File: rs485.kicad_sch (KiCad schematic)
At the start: 38 parts, among them J1801 RS485 RX Socket, J1802 RS485 TX Socket, U1801 ISO7721DR, U1802 SN75176BDR, U1803 SN75176BDR

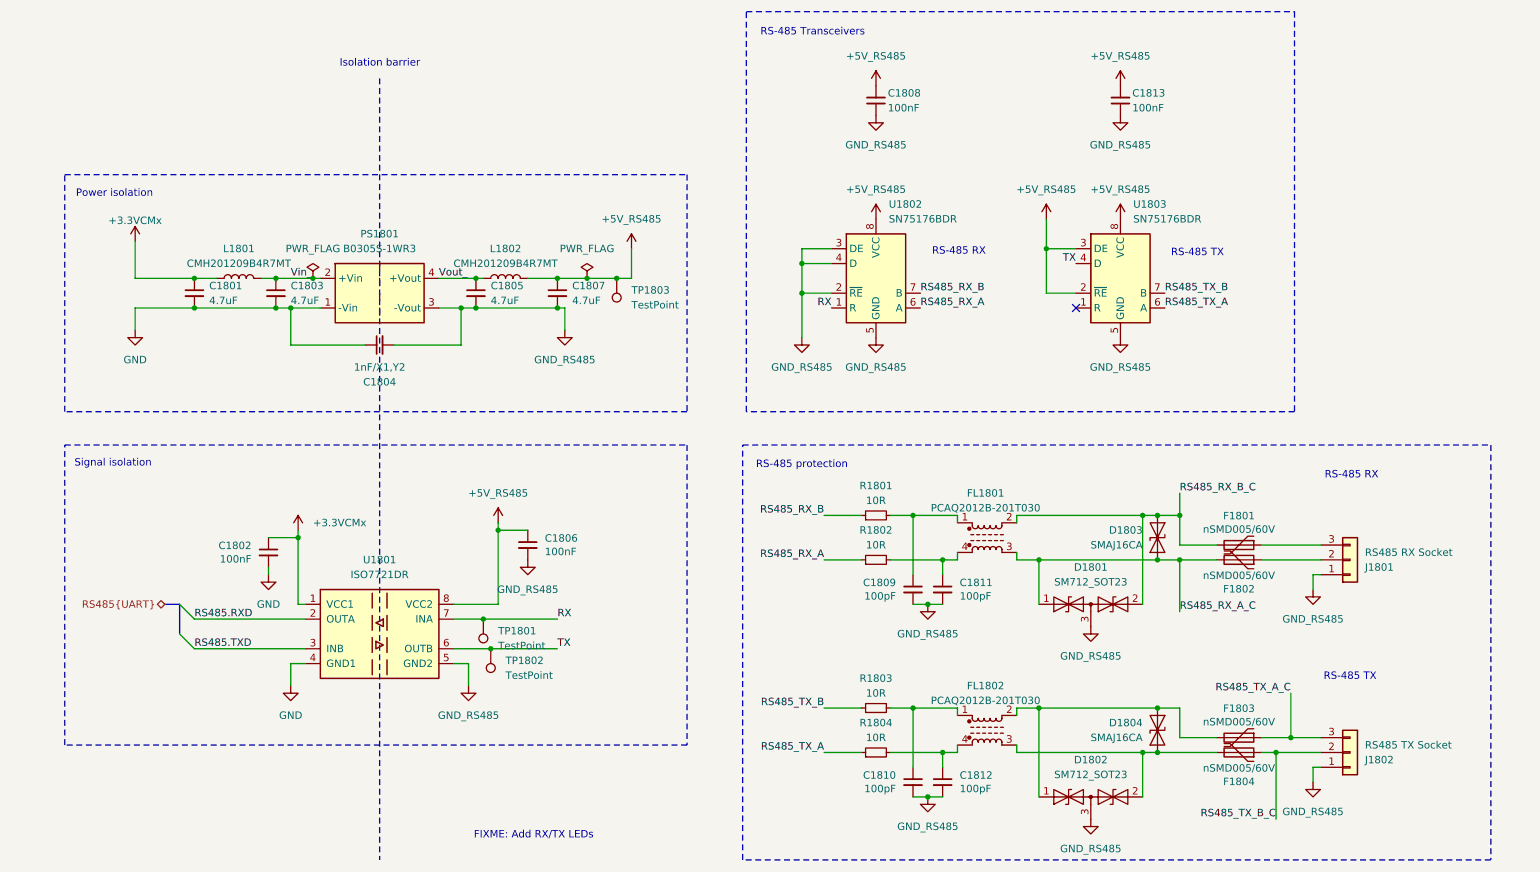
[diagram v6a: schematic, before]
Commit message: Partial trace layout, kick-ass custom rules
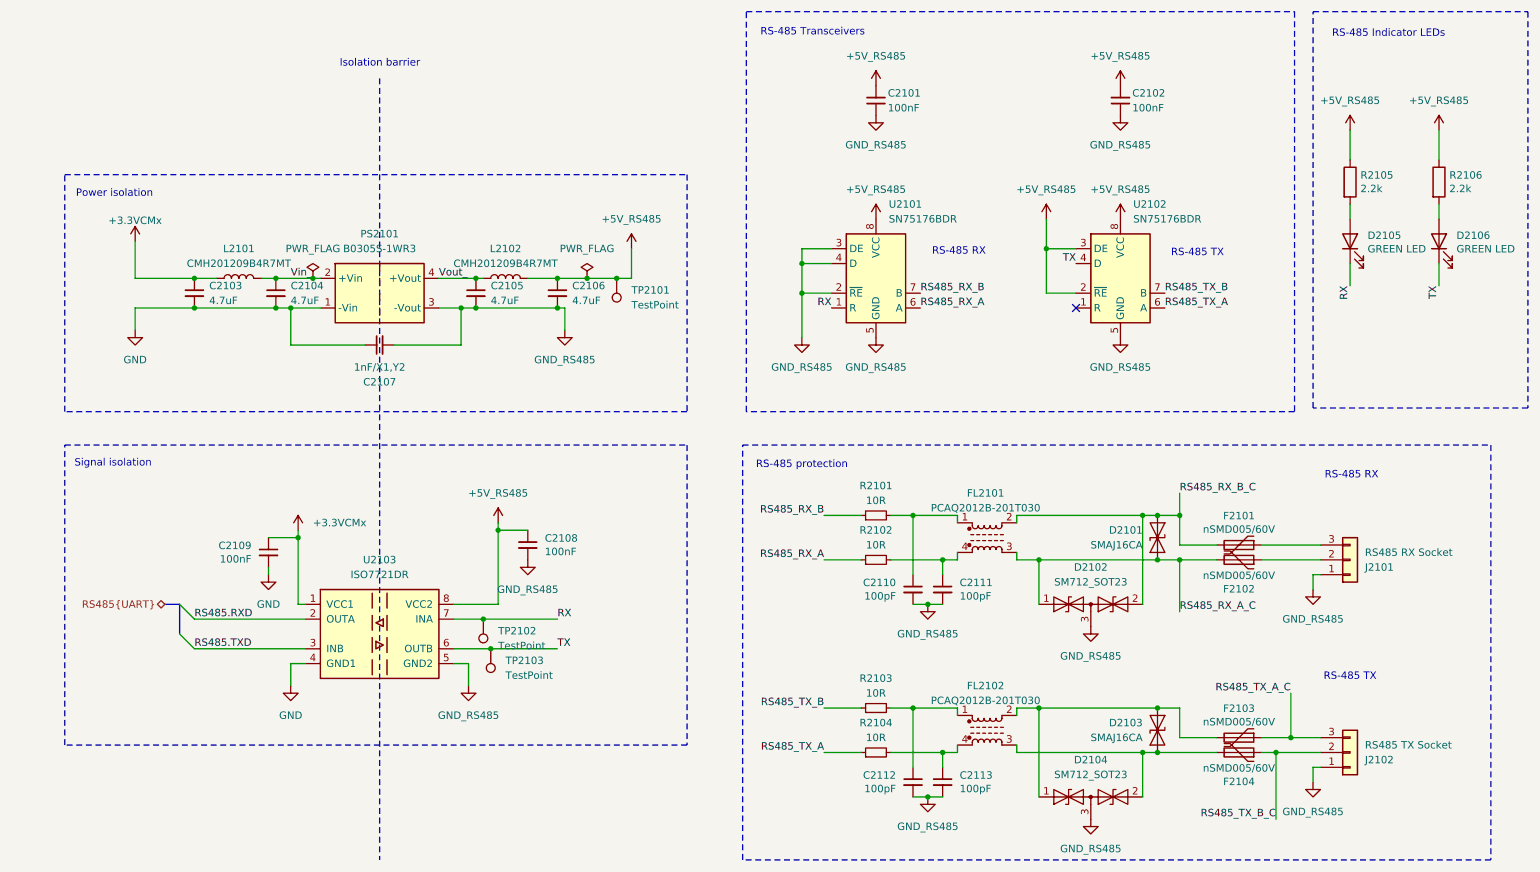
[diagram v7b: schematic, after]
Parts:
- added D2105, D2106: GREEN LED, LED_SMD:LED_0603_1608Metric, symbol Device:LED
- added R2105, R2106: 2.2k, Resistor_SMD:R_0402_1005Metric, symbol Device:R
- renumbered C1808 to C2101, C1813 to C2102, C1801 to C2103, C1803 to C2104, C1805 to C2105, C1807 to C2106, C1804 to C2107, C1806 to C2108, C1802 to C2109, C1809 to C2110, C1811 to C2111, C1810 to C2112, C1812 to C2113, D1803 to D2101, D1801 to D2102, D1804 to D2103, D1802 to D2104, F1801 to F2101, F1802 to F2102, F1803 to F2103, F1804 to F2104, FL1801 to FL2101, FL1802 to FL2102, J1801 to J2101, J1802 to J2102, L1801 to L2101, L1802 to L2102, PS1801 to PS2101, R1801 to R2101, R1802 to R2102, R1803 to R2103, R1804 to R2104, TP1803 to TP2101, TP1801 to TP2102, TP1802 to TP2103, U1802 to U2101, U1803 to U2102, U1801 to U2103
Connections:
- net +5V_RS485: now also R2105.1, R2106.1
- net RX: now also D2105.1 (K)
- net TX: now also D2106.1 (K)
- new net: D2105.2 (A), R2105.2
- new net: D2106.2 (A), R2106.2
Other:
- note added: "RS-485 Indicator LEDs"
- note removed: "FIXME: Add RX/TX LEDs"

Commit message: A big part of layout and routing done
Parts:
- removed J2102: RS485 TX Socket, Connector_Phoenix_MC:PhoenixContact_MCV_1,5_3-G-3.81_1x03_P3.81mm_Vertical, symbol Connector_Generic:Conn_01x03
- removed U2101, U2102: SN75176BDR, PCM_Package_SO_AKL:SOIC-8_3.9x4.9mm_P1.27mm, symbol Interface_UART:SN75176AD
- removed U2103: ISO7721DR, Package_SO:SOIC-8_3.9x4.9mm_P1.27mm, symbol Hatlabs:ISO7721DR
- added U2102: ISO7741DBQ, Package_SO:SSOP-16_3.9x4.9mm_P0.635mm, symbol Hatlabs:ISO7741DBQ
- added U2104, U2105: SP3485EN-L/TR, Package_SO:SOIC-8_3.9x4.9mm_P1.27mm, symbol Interface_UART:SP3485EN
- D2102: footprint PCM_Package_TO_SOT_SMD_AKL:SOT-23 -> Package_TO_SOT_SMD:SOT-23; Component Class (none) -> fine_pitch
- D2104: footprint PCM_Package_TO_SOT_SMD_AKL:SOT-23 -> Package_TO_SOT_SMD:SOT-23
- F2101, F2102, F2103, F2104: footprint PCM_Fuse_AKL:Fuse_1206_3216Metric -> Fuse:Fuse_1206_3216Metric
- J2101: value RS485 RX Socket -> RS485 Socket; footprint Connector_Phoenix_MC:PhoenixContact_MCV_1,5_3-G-3.81_1x03_P3.81mm_Vertical -> Connector_Phoenix_MC:PhoenixContact_MCV_1,5_5-G-3.81_1x05_P3.81mm_Vertical; symbol Connector_Generic:Conn_01x03 -> Connector_Generic:Conn_01x05; JLCPCB_CORRECTION 3.81;0;180 -> (none); LCSC C8389 -> C8391
- PS2101: footprint Converter_DCDC:Converter_DCDC_Murata_MEE1SxxxxSC_THT -> Hatlabs:SIP-4_L11.7-W6.0-P2.54_B0305S-1WR3
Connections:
- net +5V_RS485: now also C2101.1, C2102.1, U2102.10 (EN2), U2102.16 (VCC2), U2104.8 (VCC), U2105.2 (~{RE}), U2105.3 (DE), U2105.8 (VCC); no longer C2101.2, C2102.2
- net GND: now also C2109.1, U2102.2 (GND1), U2102.5 (INC), U2102.8 (GND1); no longer C2109.2
- net RS485.RXD: now also U2102.6 (OUTD)
- net RS485.TXD: now also U2102.3 (INA)
- net RX: now also U2102.11 (IND), U2104.1 (RO)
- net TX: now also U2102.14 (OUTA), U2105.4 (DI)
- net RX_B_: now reaches C2110.1, FL2101.1, R2101.2
- net RX_A_: now reaches C2111.1, FL2101.4, R2102.2
- net TX_B_: now reaches C2112.1, FL2102.1, R2103.2
- net RX_A_C: now reaches F2102.1, J2101.2 (Pin_2)
- net RX_B_C: now reaches F2101.1, J2101.3 (Pin_3)
- net TX_B_C_: now reaches D2103.2 (A2), D2104.1 (A1), F2103.2, FL2102.2
- net TX_A_C_: now reaches D2103.1 (A1), D2104.2 (A2), F2104.2, FL2102.3
- net TX_A_: now reaches C2113.1, FL2102.4, R2104.2
- net +3.3VCMx renamed +3.3V
- net +3.3V: now also C2109.2, U2102.1 (VCC1), U2102.7 (EN1); no longer C2109.1
- net GND_RS485 renamed GND2
- net GND2: now also C2101.2, C2102.2, U2102.15 (GND2), U2102.9 (GND2), U2104.2 (~{RE}), U2104.3 (DE), U2104.4 (DI), U2104.5 (GND), U2105.5 (GND); no longer C2101.1, C2102.1
- net RS485_RX_A renamed RX_A
- net RX_A: now also U2104.6 (A)
- net RS485_RX_A_C renamed RX_A_C_
- net RX_A_C_: now also D2102.2 (A2); no longer D2102.1 (A1)
- net RS485_RX_B renamed RX_B
- net RX_B: now also U2104.7 (B)
- net RS485_RX_B_C renamed RX_B_C_
- net RX_B_C_: now also D2102.1 (A1); no longer D2102.2 (A2)
- net RS485_TX_A renamed TX_A
- net TX_A: now also U2105.6 (A)
- net RS485_TX_A_C renamed TX_B_C
- net TX_B_C: now also J2101.5 (Pin_5)
- net RS485_TX_B renamed TX_B
- net TX_B: now also U2105.7 (B)
- net RS485_TX_B_C renamed TX_A_C
- net TX_A_C: now also J2101.4 (Pin_4)
- new net EN: U2102.13 (OUTB)
- new net RS485.EN: U2102.4 (INB)
- no-connect marks 1 -> 2
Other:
- note added: "FIXME: Connect EN to CM5 Module"
- note added: "Terminal Connector"
- moved on the sheet: C2101, C2102, C2108, C2109, TP2102, TP2103
